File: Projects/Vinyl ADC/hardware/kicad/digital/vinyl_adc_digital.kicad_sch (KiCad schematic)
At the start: 13 parts, among them J1 CLK SEL, J2 TO PI GPIO, J4 2x6 IDC, U3 74HCT132, U4 74HC4040, U6 74HC157, U8 74HC4049, X1 6.144MHz

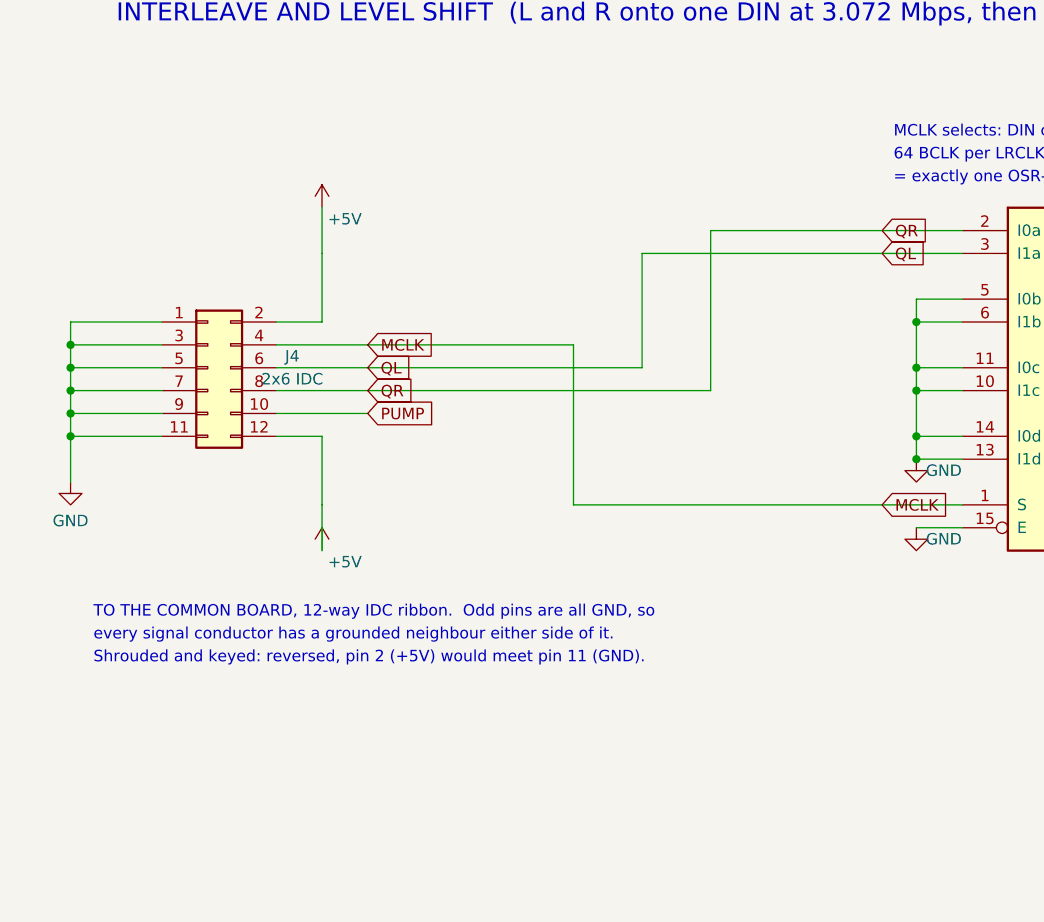
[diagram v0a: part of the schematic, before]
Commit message: Vinyl ADC: rebuild as three stacking boards
The four-board split fixed the ground plane and not the congestion --
45 wire bridges became 42, and the bridge count barely moved however the
blocks were arranged. So this moves the cut lines rather than adding more
boards.

Each channel board now carries its own 74HC74 and 74HC04, so the modulator
loop closes on one board instead of crossing a ribbon. Measured on the old
common board, 59 of its 84 F.Cu segments were per-channel CMP/DAC/Q traffic;
that is what leaves with them. The TL074 becomes two TL072s per channel, so
the integrator pairs can sit apart instead of seventeen resistors competing
for one package's perimeter. What remains of the common board is power and
the reference, so it is now vinyl_adc_power.

The five IDC ribbons become one 2x8 stacking bus -- same pinout, same
coordinates on every board, 11 mm standoffs. ONE position, not a socket and
a header side by side: a middle board has to present a socket upwards and
pins downwards at the same XY, and two separate parts cannot do that on a
single-sided board. Both channel boards are still one artwork, so nothing on
the copper may name a channel: the flip-flop drives a neutral Q_OUT and a
shunt maps it to QL or QR.

Boards are 100x100 with four M3 holes and the bus locked on the centreline,
ground row outermost so the signals open into the board rather than the edge.
pcb_fixture.py stamps that geometry; check_fixture.py proves the three
artworks still agree, testing pad position AND pin number -- a board left
un-rotated still bolts onto the standoffs and puts +5V across the ground
column.

Every project gets its own directory. KiCad resolves fp-lib-table, the
session state and ${KIPRJMOD} from the project folder, so five projects
sharing one directory made them fight over it.

pcb_link.py stamps each footprint with its schematic symbol UUID.
pcb_build.py never wrote them, so cross-probing had never worked on this
project at all -- the board is otherwise valid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
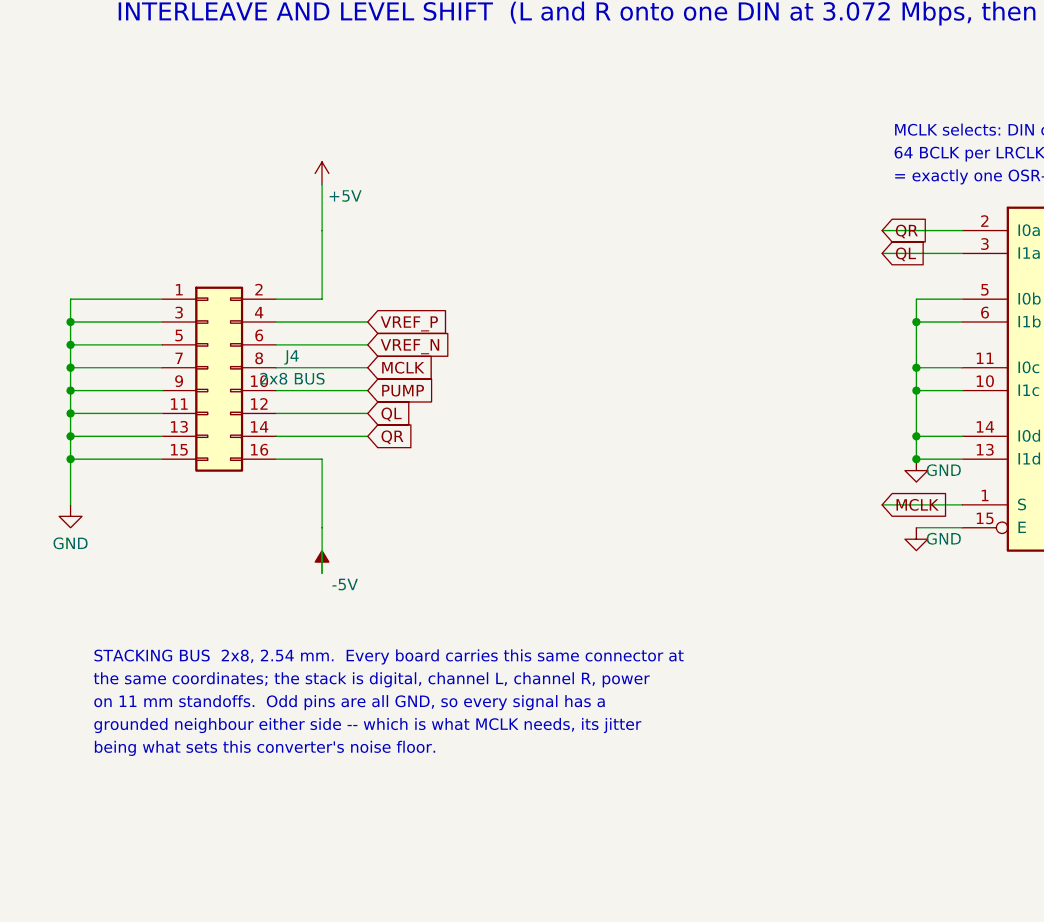
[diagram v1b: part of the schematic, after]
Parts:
- removed J4: 2x6 IDC, Connector_IDC:IDC-Header_2x06_P2.54mm_Vertical, symbol Connector_Generic:Conn_02x06_Odd_Even
- added J4: 2x8 BUS, Connector_PinHeader_2.54mm:PinHeader_2x08_P2.54mm_Vertical, symbol Connector_Generic:Conn_02x08_Odd_Even
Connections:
- net +5V: now also J4.2 (Pin_2)
- net GND: now also J4.1 (Pin_1), J4.11 (Pin_11), J4.13 (Pin_13), J4.15 (Pin_15), J4.3 (Pin_3), J4.5 (Pin_5), J4.7 (Pin_7), J4.9 (Pin_9)
- net MCLK: now also J4.8 (Pin_8)
- net PUMP: now also J4.10 (Pin_10)
- net QL: now also J4.12 (Pin_12)
- net QR: now also J4.14 (Pin_14)
- new net -5V: J4.16 (Pin_16)
- new net VREF_N: J4.6 (Pin_6)
- new net VREF_P: J4.4 (Pin_4)
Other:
- note added: "STACKING BUS 2x8, 2.54 mm. Every board carries this same connector at"
- note added: "being what sets this converter's noise floor."
- note added: "grounded neighbour either side -- which is what MCLK needs, its jitter"
- note added: "on 11 mm standoffs. Odd pins are all GND, so every signal has a"
- note added: "the same coordinates; the stack is digital, channel L, channel R, power"
- note removed: "Shrouded and keyed: reversed, pin 2 (+5V) would meet pin 11 (GND)."
- note removed: "TO THE COMMON BOARD, 12-way IDC ribbon. Odd pins are all GND, so"
- note removed: "every signal conductor has a grounded neighbour either side of it."
